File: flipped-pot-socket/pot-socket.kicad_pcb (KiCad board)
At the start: 2 copper layers, 11.5 x 22 mm, 4 parts, among them J1 Conn_01x03

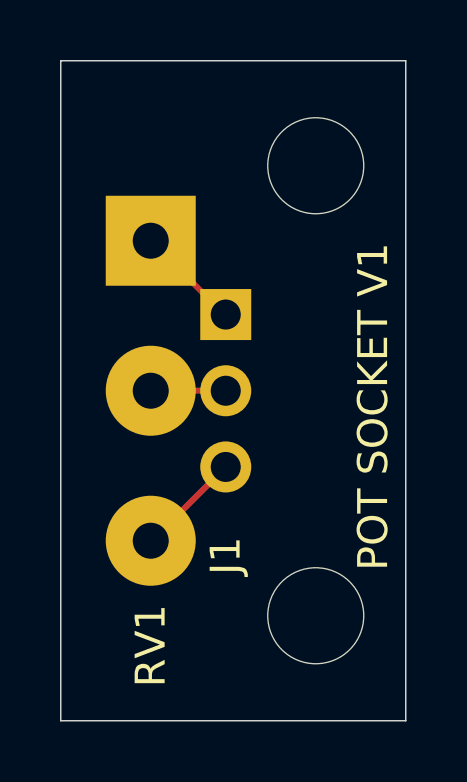
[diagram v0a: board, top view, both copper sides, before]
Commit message: Add oscillator
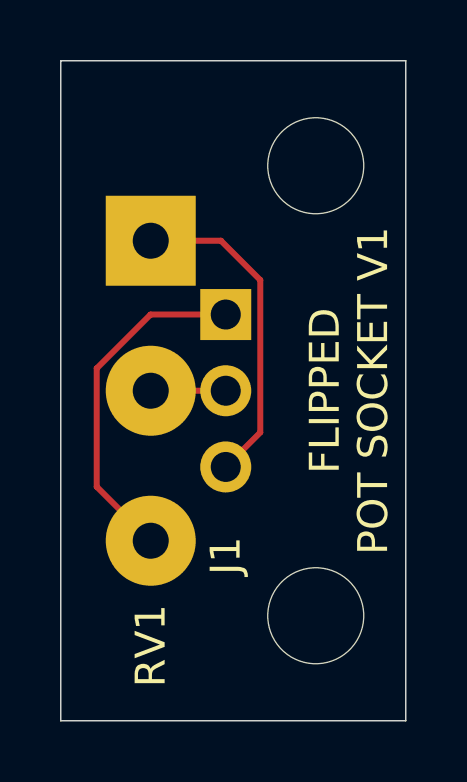
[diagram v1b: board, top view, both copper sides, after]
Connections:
- RV1 pad 1: Net-(J1-Pin_1) -> Net-(J1-Pin_3)
- RV1 pad 3: Net-(J1-Pin_3) -> Net-(J1-Pin_1)
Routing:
- net Net-(J1-Pin_1): track 3.52 -> 11.6 mm
- net Net-(J1-Pin_3): track 3.52 -> 10.9 mm
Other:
- board text added: "FLIPPED POT SOCKET V1"
- board text removed: "POT SOCKET V1"
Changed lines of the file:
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@@
 			(layers "*.Cu" "*.Mask")
 			(remove_unused_layers no)
-			(net 3 "Net-(J1-Pin_1)")
+			(net 1 "Net-(J1-Pin_3)")
 			(pinfunction "1")
 			(pintype "passive")
@@
 			(layers "*.Cu" "*.Mask")
 			(remove_unused_layers no)
-			(net 1 "Net-(J1-Pin_3)")
+			(net 3 "Net-(J1-Pin_1)")
 			(pinfunction "3")
 			(pintype "passive")
@@
 		(layer "Edge.Cuts")
 	)
-	(gr_text "POT SOCKET V1"
-		(at 155.5 106 90)
+	(gr_text "FLIPPED\nPOT SOCKET V1"
+		(at 155.5 100 90)
 		(layer "F.SilkS")
 		(effects
@@
 				(thickness 0.1)
 			)
-			(justify left bottom)
+			(justify bottom)
 		)
 	)
@@
 	)
 	(segment
+		(start 149.842 95)
+		(end 151.151 96.309)
+		(width 0.2)
+		(layer "F.Cu")
+		(net 1)
+	)
+	(segment
+		(start 151.151 96.309)
+		(end 151.151 101.389)
+		(width 0.2)
+		(layer "F.Cu")
+		(net 1)
+	)
+	(segment
+		(start 151.151 101.389)
+		(end 150 102.54)
+		(width 0.2)
+		(layer "F.Cu")
+		(net 1)
+	)
+	(segment
+		(start 147.5 95)
+		(end 149.842 95)
+		(width 0.2)
+		(layer "F.Cu")
+		(net 1)
+	)
+	(segment
+		(start 150 100)
+		(end 147.5 100)
+		(width 0.2)
+		(layer "F.Cu")
+		(net 2)
+	)
+	(segment
 		(start 147.54 105)
 		(end 147.5 105)
 		(width 0.2)
 		(layer "F.Cu")
-		(net 1)
-	)
-	(segment
-		(start 150 102.54)
-		(end 147.54 105)
-		(width 0.2)
-		(layer "F.Cu")
-		(net 1)
-	)
-	(segment
-		(start 150 100)
-		(end 147.5 100)
-		(width 0.2)
-		(layer "F.Cu")
-		(net 2)
-	)
-	(segment
-		(start 150 97.46)
-		(end 149.96 97.46)
-		(width 0.2)
-		(layer "F.Cu")
 		(net 3)
 	)
 	(segment
-		(start 149.96 97.46)
-		(end 147.5 95)
-		(width 0.2)
-		(layer "F.Cu")
+		(start 147.493001 97.46)
+		(end 150 97.46)
+		(width 0.2)
+		(layer "F.Cu")
+		(net 3)
+	)
+	(segment
+		(start 145.699 103.199)
+		(end 145.699 99.254001)
+		(width 0.2)
+		(layer "F.Cu")
+		(net 3)
+	)
+	(segment
+		(start 145.699 99.254001)
+		(end 147.493001 97.46)
+		(width 0.2)
+		(layer "F.Cu")
+		(net 3)
+	)
+	(segment
+		(start 147.5 105)
+		(end 145.699 103.199)
+		(width 0.2)
+		(layer "F.Cu")
